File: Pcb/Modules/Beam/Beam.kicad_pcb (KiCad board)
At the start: 2 copper layers, 25 x 47.9 mm, 23 parts, among them J1 Conn_01x02, J2 Conn_01x04, Q1 BC817, U1 LMC555xM, U2 LM358, U3 TSOP585xx

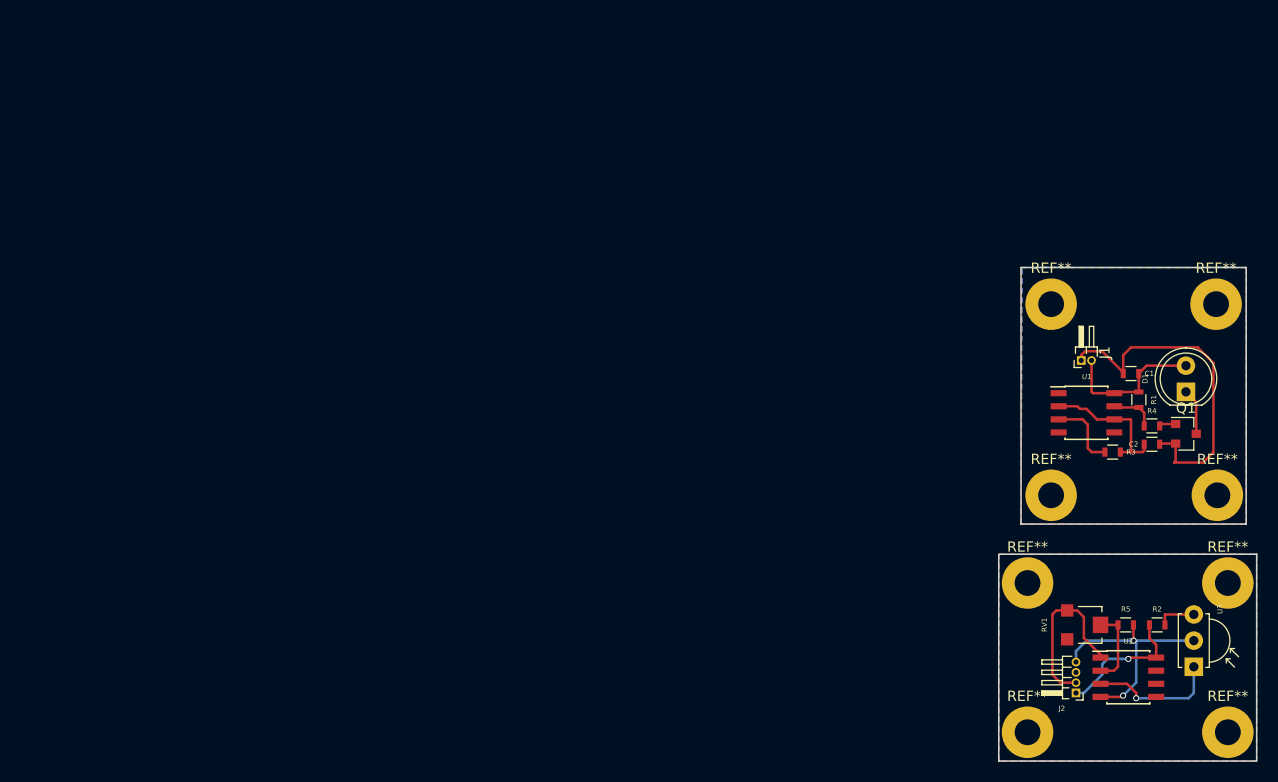
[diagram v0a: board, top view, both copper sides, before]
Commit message: Pcb layout for beam and projectile module
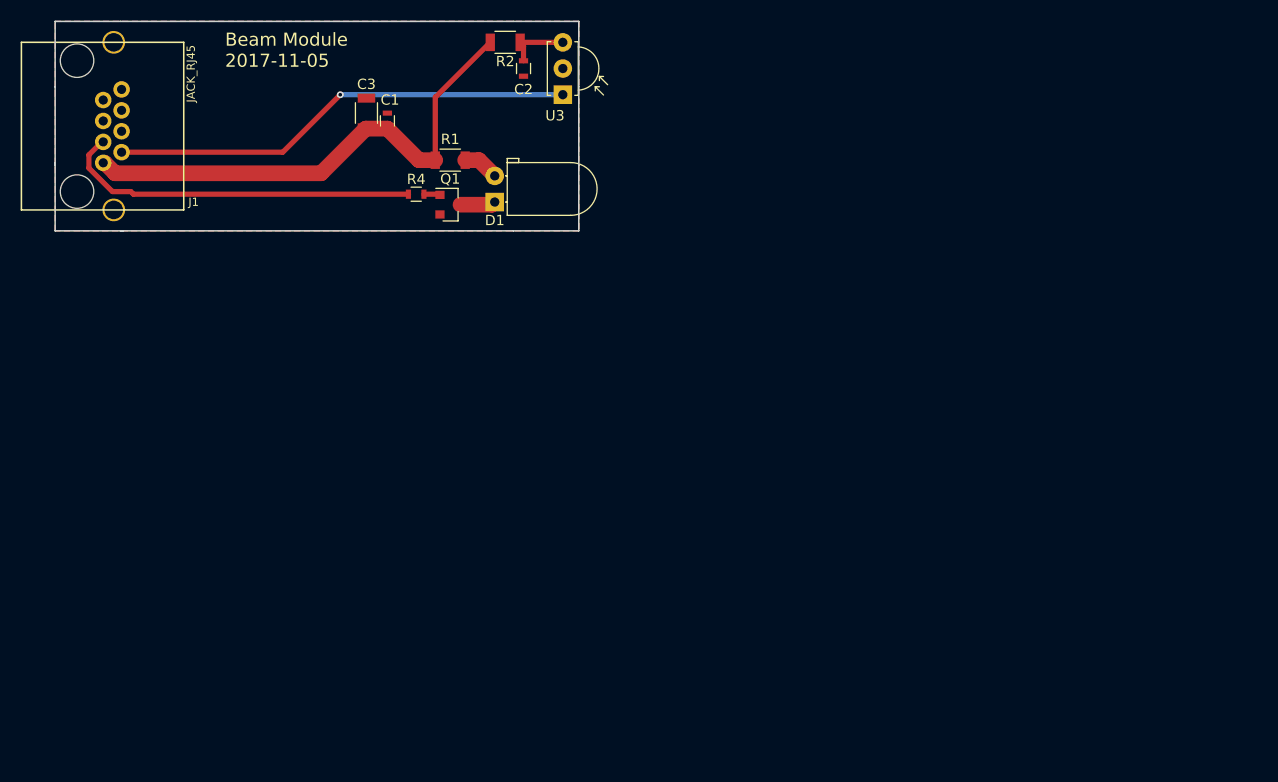
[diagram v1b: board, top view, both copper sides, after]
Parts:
- removed J2: Conn_01x04, Pin_Headers:Pin_Header_Angled_1x04_Pitch1.00mm
- removed R3, R5: R, Resistors_SMD:R_0603
- removed REF** (x8): MountingHole_2.5mm_Pad, Mounting_Holes:MountingHole_2.5mm_Pad
- removed RV1: POT, Potentiometers:Potentiometer_Trimmer-EVM3E
- removed U1: LMC555xM, Housings_SOIC:SOIC-8_3.9x4.9mm_Pitch1.27mm
- removed U2: LM358, Housings_SOIC:SOIC-8_3.9x4.9mm_Pitch1.27mm
- added C3: 10uF, Resistors_SMD:R_1206, F.Cu at (65.8, 44.5)
- C1, C2: value C_Small -> 0.1uF
- D1: value LD274 -> IR_LED; footprint LEDs:LED_D5.0mm -> LEDs:LED_D5.0mm_Horizontal_O1.27mm_Z15.0mm
- J1: value Conn_01x02 -> JACK_RJ45; footprint Pin_Headers:Pin_Header_Angled_1x02_Pitch1.00mm -> CA6:RJ45_pcbwing
- Q1: value BC817 -> Q_NMOS_GSD
- R1, R2: value R -> 20R; footprint Resistors_SMD:R_0603 -> Resistors_SMD:R_1206
- R4: value R -> 1K
- moved J1 97.7 mm to (40.1, 45.7), turned to 270 degrees
- moved R2 84.8 mm to (79.2, 37.6), turned to 180 degrees
- moved U3 82.6 mm to (84.8, 42.7)
- moved C1 76.2 mm to (67.8, 45.2), turned to 90 degrees
- moved R4 74.8 mm to (70.6, 52.3)
- moved Q1 74.8 mm to (73.9, 53.3)
- moved C2 71.0 mm to (81.0, 40.1), turned to 270 degrees
- moved R1 70.7 mm to (73.9, 49.0), turned to 180 degrees
- moved D1 69.5 mm to (78.2, 53.1)
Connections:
- C1 pad 1: Net-(C1-Pad1) -> +3V3
- C1 pad 2: Net-(C1-Pad2) -> GND
- C2 pad 2: Net-(C1-Pad2) -> GND
- D1 pad 2: Net-(C1-Pad1) -> Net-(D1-Pad2)
- J1 pad 1: Net-(C1-Pad2) -> +3V3
- J1 pad 2: Net-(C1-Pad1) -> Net-(J1-Pad2)
- Q1 pad 2: Net-(C1-Pad2) -> GND
- R1 pad 1: Net-(C1-Pad1) -> Net-(D1-Pad2)
- R1 pad 2: Net-(R1-Pad2) -> +3V3
- R2 pad 1: Net-(J2-Pad1) -> Net-(C2-Pad1)
- R2 pad 2: Net-(R2-Pad2) -> +3V3
- R4 pad 1: Net-(R1-Pad2) -> Net-(J1-Pad3)
- U3 pad 1: Net-(U2-Pad3) -> Net-(J1-Pad2)
- U3 pad 2: Net-(J2-Pad4) -> GND
- U3 pad 3: Net-(R2-Pad2) -> Net-(C2-Pad1)
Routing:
- net +3V3: track 0.00 -> 49.3 mm
- net Net-(J1-Pad2): track 0.00 -> 45.1 mm, vias 0 -> 1
- net Net-(J1-Pad3): track 0.00 -> 35.2 mm
- net Net-(C1-Pad2): track 33.5 -> 0.00 mm
- net Net-(J2-Pad4): track 22.7 -> 0.00 mm, vias 2 -> 0
- net Net-(J2-Pad2): track 16.5 -> 0.00 mm
- net Net-(C1-Pad1): track 14.4 -> 0.00 mm
- net Net-(J2-Pad1): track 13.2 -> 0.00 mm, vias 1 -> 0
- net Net-(U2-Pad3): track 12.7 -> 0.00 mm, vias 1 -> 0
- net Net-(C2-Pad1): track 13.7 -> 6.06 mm
- net Net-(R5-Pad2): track 7.60 -> 0.00 mm
- net Net-(R3-Pad2): track 7.14 -> 0.00 mm
- net Net-(R1-Pad2): track 4.43 -> 0.00 mm
- net Net-(R2-Pad2): track 3.81 -> 0.00 mm
- net Net-(D1-Pad2): track 0.00 -> 3.50 mm
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- added copper zone on B.Cu, net GND
- removed copper zone on B.Cu, net (none)
- removed copper zone on F.Cu, net (none)
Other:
- board size 25 x 47.9 mm -> 50.8 x 20.3 mm
- net class Default: clearance 0.2 -> 0.254; trace_width 0.25 -> 0.254; via_dia 0.6 -> 0.6604; via_drill 0.4 -> 0.3556
- rule trace_clearance: 0.2 -> 0.254
- board text added: "Beam Module 2017-11-05"

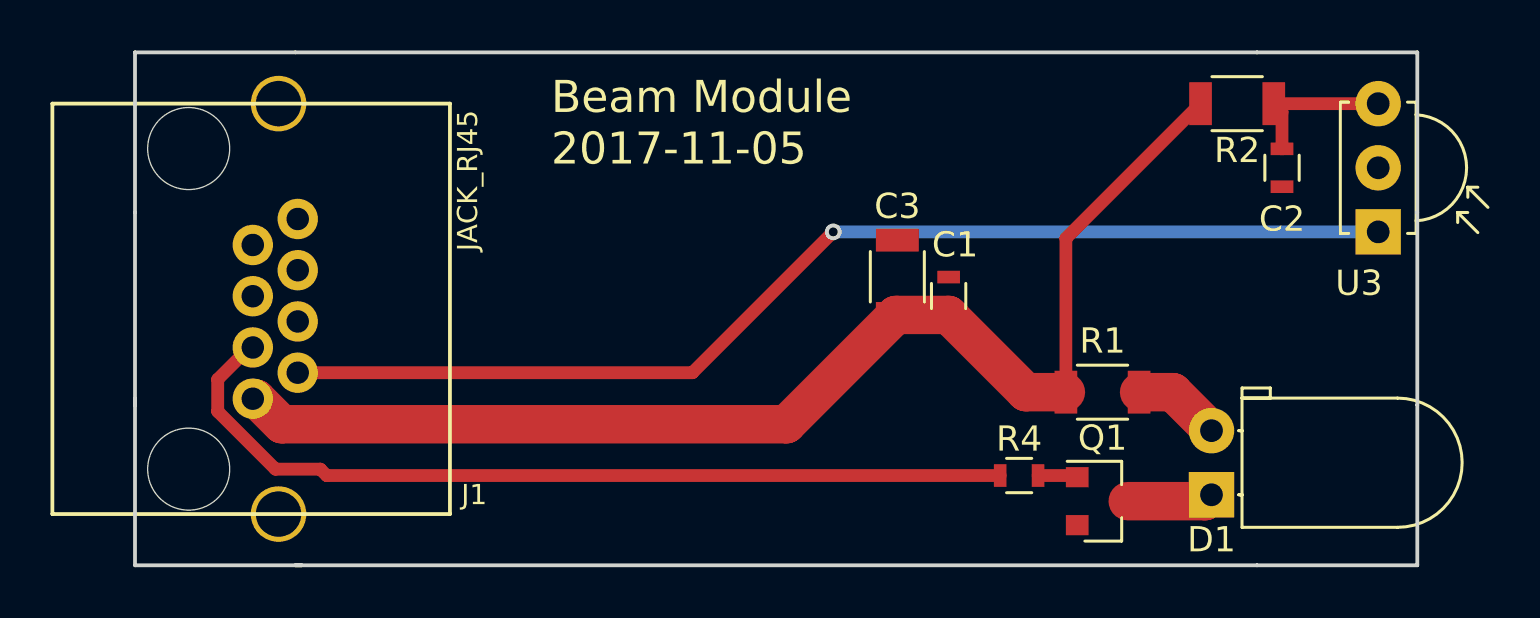
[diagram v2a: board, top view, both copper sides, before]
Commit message: Update module pcbs
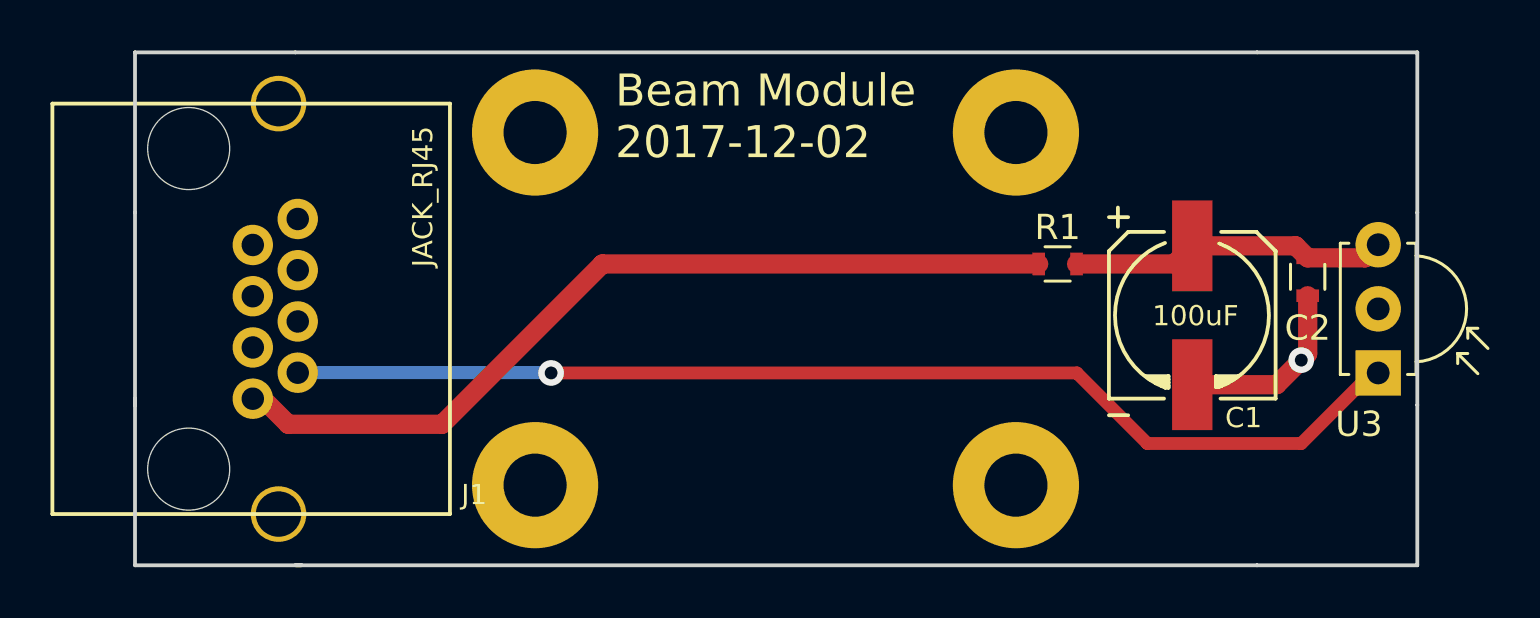
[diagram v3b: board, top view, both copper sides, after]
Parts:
- removed C3: 10uF, Resistors_SMD:R_1206
- removed D1: IR_LED, LEDs:LED_D5.0mm_Horizontal_O1.27mm_Z15.0mm
- removed Q1: Q_NMOS_GSD, TO_SOT_Packages_SMD:SOT-23
- removed R2: 20R, Resistors_SMD:R_1206
- removed R4: 1K, Resistors_SMD:R_0603
- added X1: HOLE, Mounting_Holes:MountingHole_2.5mm_Pad, F.Cu at (51.4, 38.7)
- added X2: HOLE, Mounting_Holes:MountingHole_2.5mm_Pad, F.Cu at (51.4, 52.7)
- added X3: HOLE, Mounting_Holes:MountingHole_2.5mm_Pad, F.Cu at (70.5, 38.7)
- added X4: HOLE, Mounting_Holes:MountingHole_2.5mm_Pad, F.Cu at (70.5, 52.7)
- C1: value 0.1uF -> 100uF; footprint Resistors_SMD:R_0603 -> CA6:c_elec_6.3x5.7
- R1: value 20R -> 100R; footprint Resistors_SMD:R_1206 -> Resistors_SMD:R_0603
- moved C1 9.68 mm to (77.5, 46.0)
- moved U3 5.59 mm to (84.8, 48.3)
- moved R1 5.38 mm to (72.1, 43.9), turned to 0 degrees
- moved C2 4.44 mm to (82.0, 44.5)
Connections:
- C1 pad 1: +3V3 -> Net-(C1-Pad1)
- C2 pad 1: Net-(C2-Pad1) -> Net-(C1-Pad1)
- J1 pad 3: Net-(J1-Pad3) -> (no net)
- R1 pad 1: Net-(D1-Pad2) -> +3V3
- R1 pad 2: +3V3 -> Net-(C1-Pad1)
- U3 pad 3: Net-(C2-Pad1) -> Net-(C1-Pad1)
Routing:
- net Net-(J1-Pad3): track 35.2 -> 0.00 mm
- net +3V3: track 49.3 -> 34.2 mm
- net Net-(C1-Pad1): track 0.00 -> 12.7 mm
- net GND: track 0.00 -> 7.38 mm, vias 0 -> 1
- net Net-(C2-Pad1): track 6.06 -> 0.00 mm
- net Net-(D1-Pad2): track 3.50 -> 0.00 mm
- net Net-(D1-Pad1): track 3.42 -> 0.00 mm
- net Net-(Q1-Pad1): track 1.58 -> 0.00 mm
- removed copper zone on F.Cu, net GND
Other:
- board text added: "Beam Module 2017-12-02"
- board text removed: "Beam Module 2017-11-05"
